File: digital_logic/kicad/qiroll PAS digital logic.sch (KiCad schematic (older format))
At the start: 41 parts, among them J1 brk_sense, J2 led_sw1, J3 Jumper, J4 mode_thr_batt, J5 pas_sense, J6 Jumper, U1 4093B, U2 4027B, U3 4093B, U5 4093B, U6 14538B, U7 L78L05_TO92

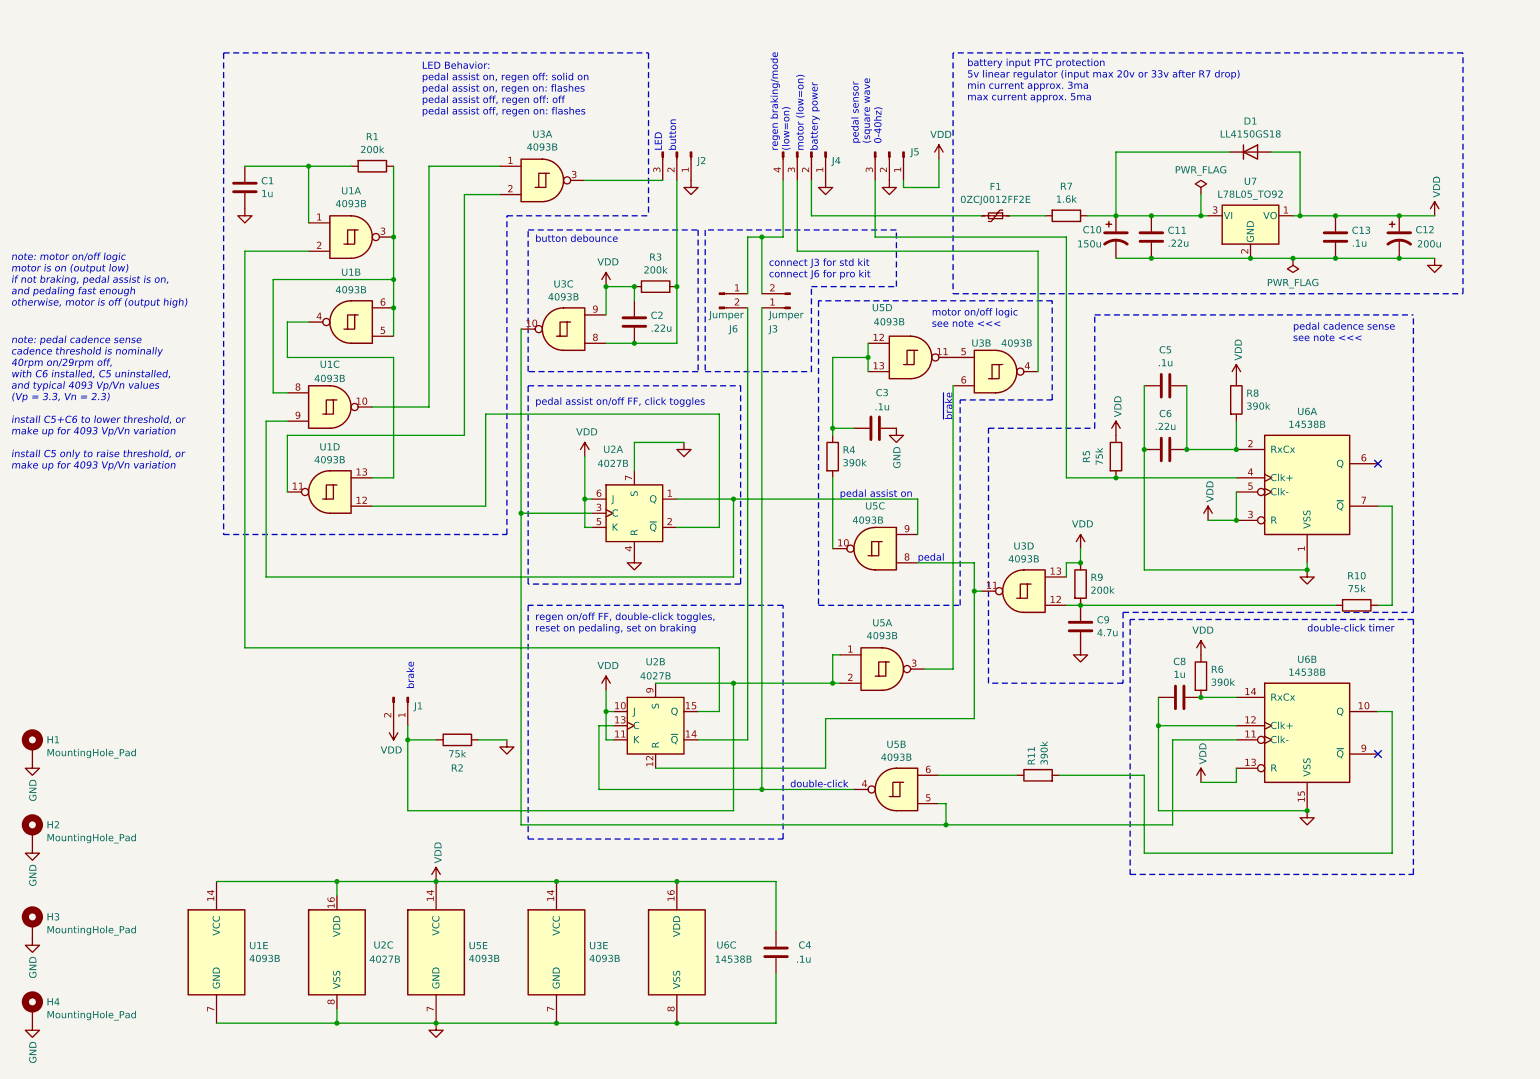
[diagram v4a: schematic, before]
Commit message: pcb version 2.2, hopefully fixes brake input/mode instablity
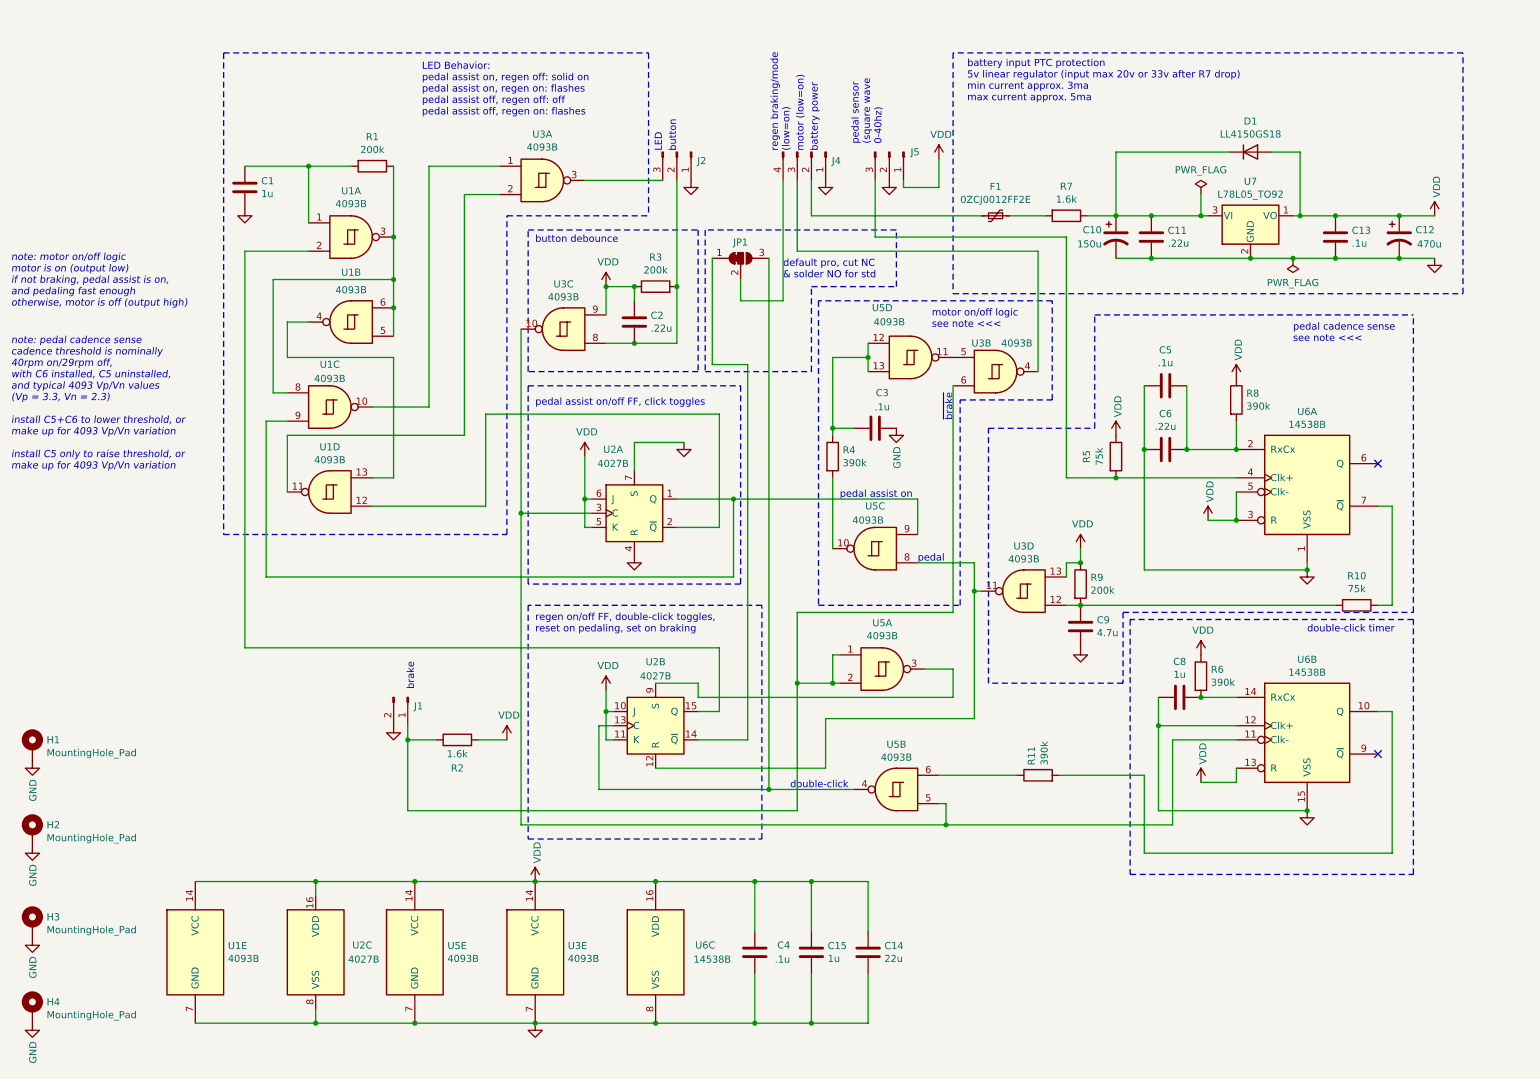
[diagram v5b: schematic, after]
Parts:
- removed J3, J6: Jumper, Connector_PinHeader_2.54mm:PinHeader_1x02_P2.54mm_Vertical, symbol Connector:Conn_01x02_Male
- added C14: 22u, Capacitor_SMD:C_0603_1608Metric, symbol Device:C
- added C15: 1u, Capacitor_SMD:C_0603_1608Metric, symbol Device:C
- added JP1: SolderJumper_3_Bridged12, Jumper:SolderJumper-3_P1.3mm_Bridged12_RoundedPad1.0x1.5mm_NumberLabels, symbol Jumper:SolderJumper_3_Bridged12
- C12: value 200u -> 470u
- R2: value 75k -> 1.6k
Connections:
- net GND: now also J1.2 (Pin_2), C14.2, C15.2; no longer R2.2
- net VDD: now also R2.2, C14.1, C15.1; no longer J1.2 (Pin_2)
- net at U2.13 (C), U5.4: now also JP1.3 (B)
- net at U2.14 (~Q): now also JP1.1 (A)
- net at J1.1 (Pin_1), R2.1, U5.1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: now also U3.6; no longer U2.9 (S)
- net at J4.4 (Pin_4): now also JP1.2 (C)
- net at U5.3: now also U2.9 (S); no longer U3.6
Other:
- note added: "default pro, cut NC\n& solder NO for std\n"
- note removed: "connect J3 for std kit\nconnect J6 for pro kit"
- moved on the sheet: C4, U1E, U2C, U3E, U5E, U6C
